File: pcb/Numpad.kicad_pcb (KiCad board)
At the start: 2 copper layers, 76.2 x 114.3 mm, 61 parts, among them P1 USB-MICRO-B, P2 HOLE, P3 HOLE, P4 HOLE, P5 HOLE, SW1 F13, SW10 8, SW11 9, SW12 PLUS, SW13 4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

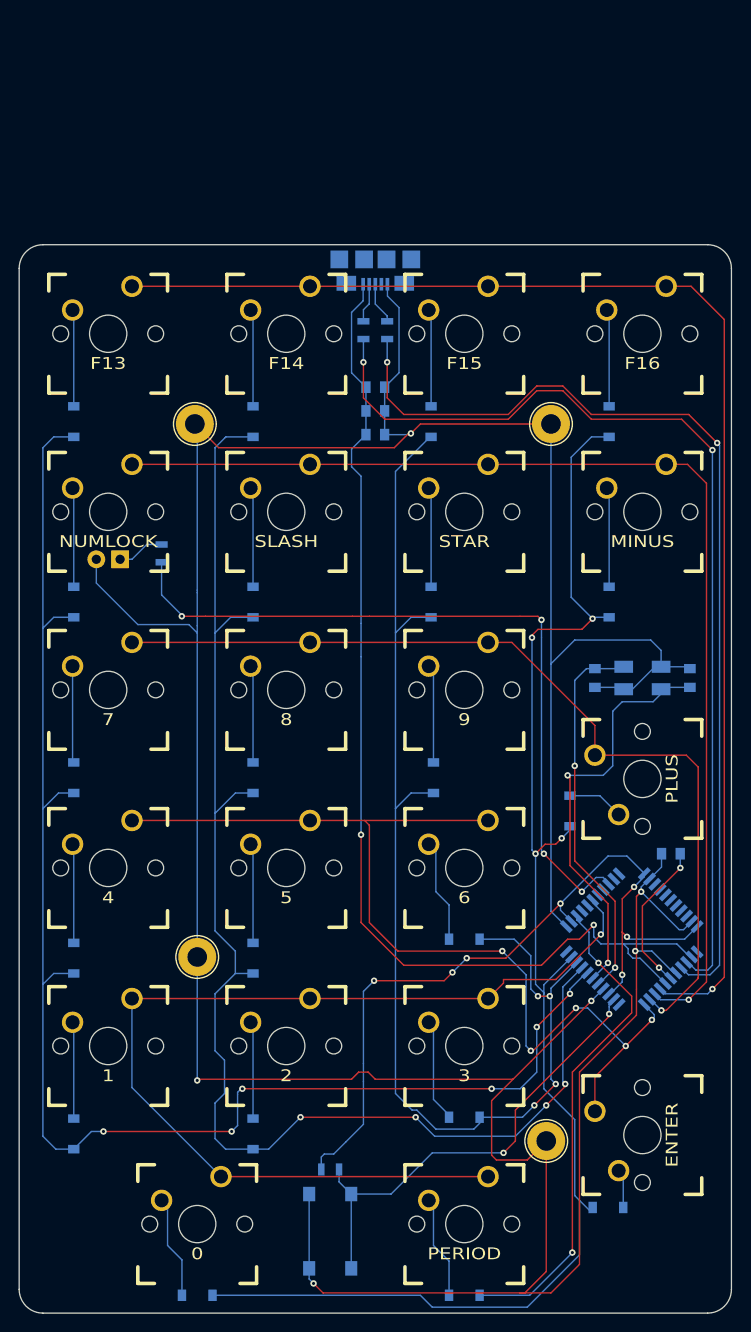
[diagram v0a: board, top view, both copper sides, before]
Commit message: Fix VCC/+5V problem. Shrink board by like 10 mils
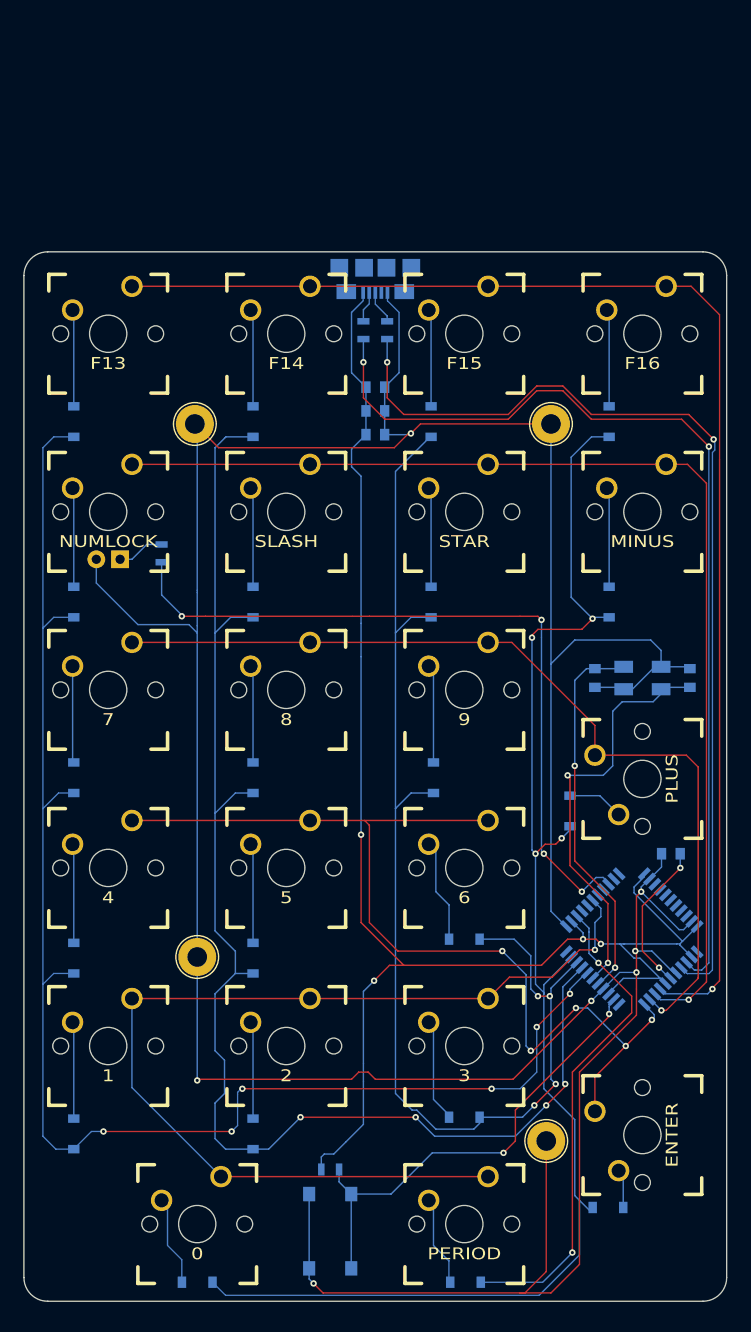
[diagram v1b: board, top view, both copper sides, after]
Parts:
- moved D21 1.40 mm to (113.8, 165.6)
- moved D20 1.40 mm to (85.1, 165.6)
- moved P1 0.89 mm to (104.1, 55.6)
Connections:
- R4 pad 2: VCC -> +5V
- U1 pad 14: VCC -> +5V
- U1 pad 24: VCC -> +5V
- U1 pad 34: VCC -> +5V
- U1 pad 44: VCC -> +5V
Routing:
- net VCC: track 84.3 -> 0.00 mm, vias 7 -> 0
- net +5V: track 118.3 -> 164.8 mm, vias 2 -> 4
- net GND: track 409.4 -> 396.9 mm, vias 6 -> 7
- net Net-(D20-Pad2): track 11.1 -> 9.66 mm
- net Net-(D21-Pad2): track 11.1 -> 9.74 mm
- net Net-(P1-Pad2): track 4.22 -> 3.33 mm
- net Net-(P1-Pad3): track 4.49 -> 3.60 mm
- net /COL4: track 52.9 -> 52.2 mm
- net Net-(R1-Pad1): track 106.9 -> 106.3 mm
- net Net-(R2-Pad1): track 106.9 -> 106.4 mm
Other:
- board size 76.2 x 114.3 mm -> 75.2 x 112.3 mm
- net class Default: clearance 0.1524 -> 0.127; trace_width 0.1524 -> 0.127
- rule trace_clearance: 0.1524 -> 0.127
- rule trace_min: 0.1524 -> 0.127

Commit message: Macrofab order
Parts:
- C2, C3: value 18p -> 8p
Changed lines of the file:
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@@
     (links 107)
     (no_connects 0)
-    (area 66.497999 55.321999 141.782001 167.690001)
+    (area 65.963799 54.123599 142.316201 168.986201)
     (thickness 1.6)
     (drawings 8)
@@
     (visible_elements 7FFFFFFF)
     (pcbplotparams
-      (layerselection 0x01000_00000000)
+      (layerselection 0x00030_00000000)
       (usegerberextensions false)
       (excludeedgelayer true)
@@
       (drillshape 0)
       (scaleselection 1)
-      (outputdirectory ../../../../../Desktop/))
+      (outputdirectory fab/))
   )
   (net 0 "")
@@
       (effects (font (size 0.5 0.5) (thickness 0.1)) (justify mirror))
     )
-    (fp_text value 18p (at -2.21 -0.01 180) (layer B.SilkS)
+    (fp_text value 8p (at -2.21 -0.01 180) (layer B.SilkS)
       (effects (font (size 0.5 0.5) (thickness 0.1)) (justify mirror))
     )
@@
       (effects (font (size 0.5 0.5) (thickness 0.1)) (justify mirror))
     )
-    (fp_text value 18p (at 2.21 -0.01 360) (layer B.SilkS)
+    (fp_text value 8p (at 2.21 -0.01 360) (layer B.SilkS)
       (effects (font (size 0.5 0.5) (thickness 0.1)) (justify mirror))
     )
@@
   (segment (start 135.61693 133.07693) (end 135.74393 133.07693) (width 0.1524) (layer B.Cu) (net 1))
   (segment (start 106.68 61.849) (end 105.44 60.609) (width 0.127) (layer B.Cu) (net 2))
-  (segment (start 105.44 60.609) (end 105.44 59.726) (width 0.127) (layer B.Cu) (net 2) (status 800000))
+  (segment (start 105.44 60.609) (end 105.44 59.726) (width 0.127) (layer B.Cu) (net 2))
   (segment (start 128.531441 134.208301) (end 130.278742 132.461) (width 0.127) (layer B.Cu) (net 2))
   (via (at 132.08 132.461) (size 0.6858) (drill 0.3302) (layers F.Cu B.Cu) (net 2))
@@
   (segment (start 127.635 99.965) (end 130.515 99.965) (width 0.1524) (layer B.Cu) (net 4))
   (segment (start 130.515 99.965) (end 130.715 99.765) (width 0.1524) (layer B.Cu) (net 4))
-  (segment (start 102.84 59.726) (end 102.84 60.609) (width 0.127) (layer B.Cu) (net 5) (status 400000))
+  (segment (start 102.84 59.726) (end 102.84 60.609) (width 0.127) (layer B.Cu) (net 5))
   (segment (start 102.84 60.609) (end 101.6 61.849) (width 0.1524) (layer B.Cu) (net 5))
   (segment (start 101.6 61.849) (end 101.6 68.31) (width 0.1524) (layer B.Cu) (net 5))
@@
   (segment (start 79.69 86.68) (end 81.28 86.68) (width 0.1524) (layer B.Cu) (net 32))
   (segment (start 78.105 88.265) (end 79.69 86.68) (width 0.1524) (layer B.Cu) (net 32))
-  (segment (start 103.49 59.726) (end 103.49 60.945) (width 0.127) (layer B.Cu) (net 33) (status 400000))
+  (segment (start 103.49 59.726) (end 103.49 60.945) (width 0.127) (layer B.Cu) (net 33))
   (segment (start 103.49 60.945) (end 102.87 61.565) (width 0.1524) (layer B.Cu) (net 33))
   (segment (start 102.87 61.565) (end 102.87 62.804) (width 0.1524) (layer B.Cu) (net 33))
-  (segment (start 104.14 59.726) (end 104.14 60.96) (width 0.127) (layer B.Cu) (net 34) (status 400000))
+  (segment (start 104.14 59.726) (end 104.14 60.96) (width 0.127) (layer B.Cu) (net 34))
   (segment (start 104.14 60.96) (end 105.41 62.23) (width 0.1524) (layer B.Cu) (net 34))
   (segment (start 105.41 62.23) (end 105.41 62.804) (width 0.1524) (layer B.Cu) (net 34))

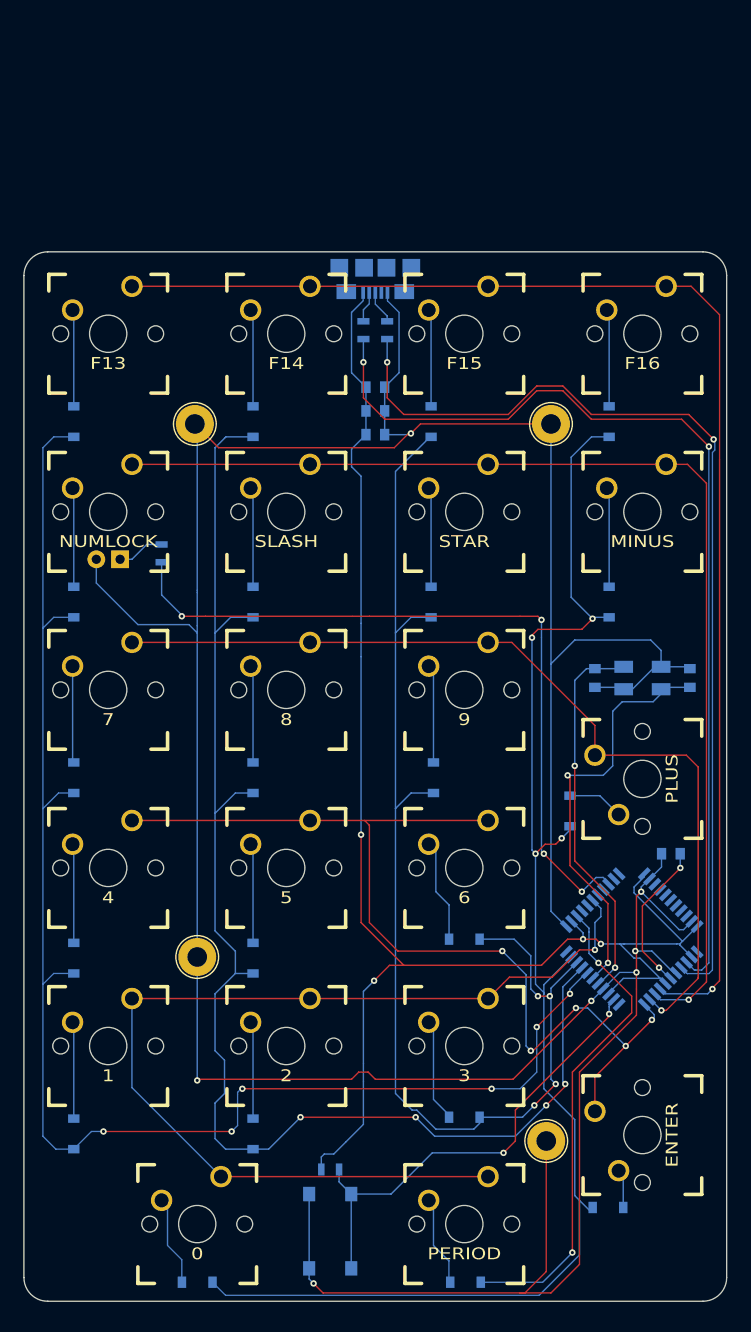
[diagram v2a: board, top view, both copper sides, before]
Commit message: Remove atmega32u4 and related components
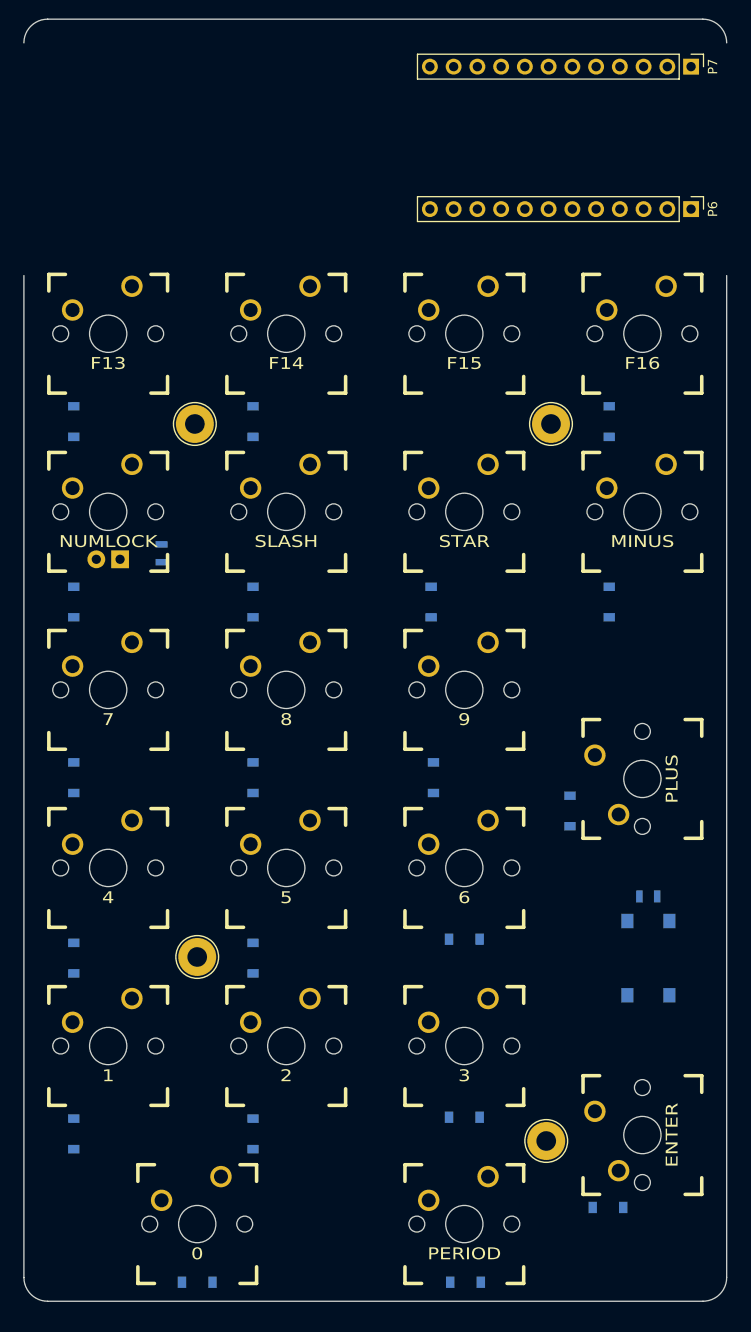
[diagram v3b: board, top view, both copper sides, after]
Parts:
- removed C1, C6: 1u, Keyboard:C_0805
- removed C2, C3: 8p, Keyboard:C_0805
- removed C4, C5: 0.1u, Keyboard:C_0805
- removed D3: D, Diodes_SMD:SOD-123
- removed P1: USB-MICRO-B, 10118192-0001LF:10118192-0001LF
- removed R1, R2: 22, Keyboard:R_0805
- removed U1: ATmega32U4-AU, ATMEGA32U4-AU:QFP80P1200X1200X120-44N
- removed X1: 16MHz, Crystals:Crystal_SMD_5032_4Pads
- added P6: CONN_01X12, Pin_Headers:Pin_Header_Straight_1x12_Pitch2.54mm, F.Cu at (137.9, 50.8)
- added P7: CONN_01X12, Pin_Headers:Pin_Header_Straight_1x12_Pitch2.54mm, F.Cu at (137.9, 35.6)
- moved R4 44.9 mm to (133.3, 124.3)
- moved SW22 44.9 mm to (133.3, 130.9)
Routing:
- net GND: track 396.9 -> 0.00 mm, vias 7 -> 0
- net +5V: track 164.8 -> 0.00 mm, vias 4 -> 0
- net /COL0: track 160.8 -> 0.00 mm, vias 6 -> 0
- net /COL3: track 154.1 -> 0.00 mm, vias 4 -> 0
- net /COL1: track 148.8 -> 0.00 mm, vias 4 -> 0
- net /ROW0: track 142.6 -> 0.00 mm, vias 1 -> 0
- net /COL2: track 128.8 -> 0.00 mm, vias 4 -> 0
- net /ROW1: track 122.2 -> 0.00 mm, vias 1 -> 0
- net /ROW4: track 109.2 -> 0.00 mm, vias 1 -> 0
- net Net-(R2-Pad1): track 106.4 -> 0.00 mm, vias 2 -> 0
- net Net-(R1-Pad1): track 106.3 -> 0.00 mm, vias 2 -> 0
- net /ROW3: track 104.9 -> 0.00 mm, vias 5 -> 0
- net /ROW2: track 97.9 -> 0.00 mm, vias 1 -> 0
- net /NUMLOCK_LED: track 80.1 -> 0.00 mm, vias 4 -> 0
- net /COL4: track 52.2 -> 0.00 mm, vias 2 -> 0
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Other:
- board size 75.2 x 112.3 mm -> 75.2 x 137.2 mm

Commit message: Complete routes and layout. Need to check Osh Park rules
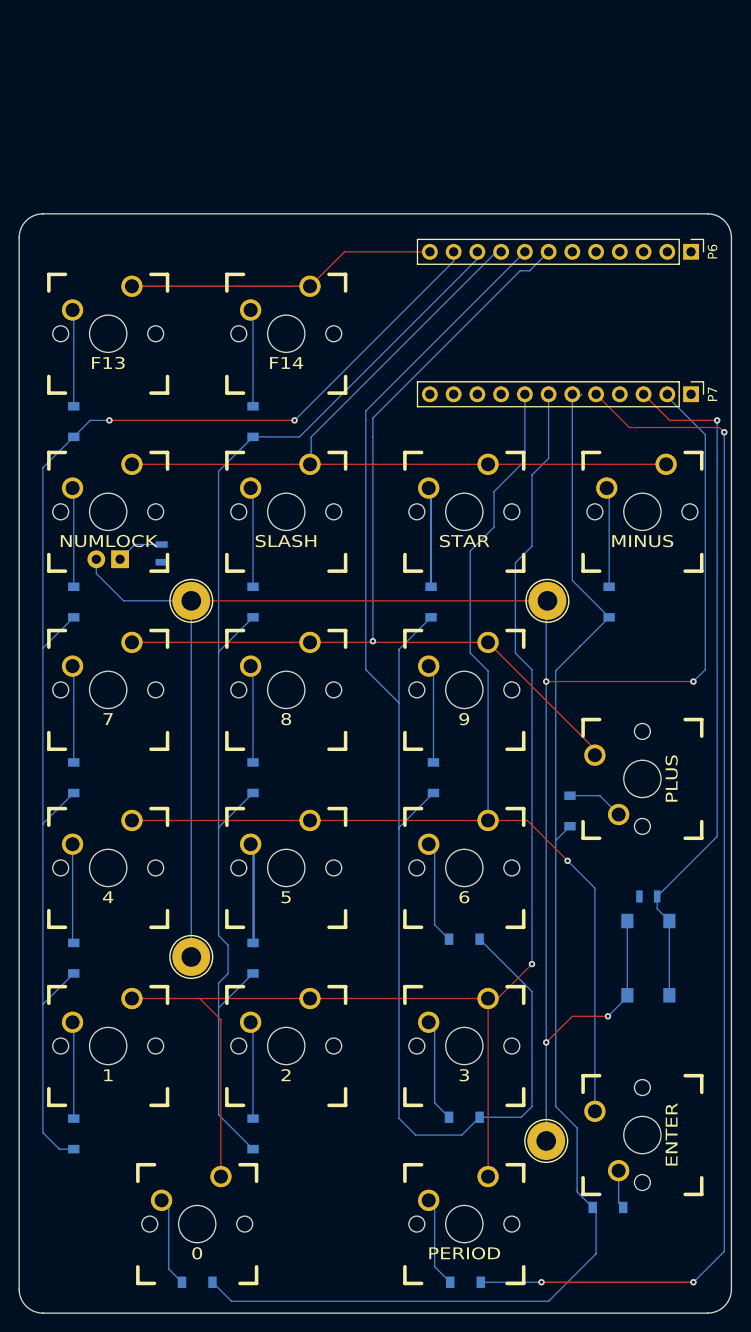
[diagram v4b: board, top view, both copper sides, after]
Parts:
- removed D4: D, Diodes_SMD:SOD-123
- removed SW3: F15, Tim's Cherry MX:CHERRY_PLATE_100H
- removed SW4: F16, Tim's Cherry MX:CHERRY_PLATE_100H
- moved P7 35.1 mm to (137.9, 70.6)
- moved P2 18.9 mm to (84.5, 92.7)
- moved P3 18.9 mm to (122.6, 92.7)
- moved P6 4.57 mm to (137.9, 55.4)
- moved P4 0.64 mm to (84.5, 130.8)
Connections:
- P6 pad 10: /ROW3 -> /COL1
- P6 pad 11: /ROW4 -> /COL0
- P6 pad 12: /COL0 -> /ROW0
- P6 pad 7: /ROW0 -> /ROW2
- P6 pad 8: /ROW1 -> /COL2
- P6 pad 9: /ROW2 -> /ROW1
- P7 pad 2: Net-(P7-Pad2) -> GND
- P7 pad 5: /COL1 -> /COL4
- P7 pad 6: /COL2 -> /COL3
- P7 pad 7: /COL3 -> /ROW4
- P7 pad 8: /COL4 -> /ROW3
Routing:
- net GND: track 0.00 -> 214.8 mm, vias 0 -> 4
- net /COL2: track 0.00 -> 153.6 mm
- net /ROW4: track 0.00 -> 146.5 mm, vias 0 -> 1
- net /COL3: track 0.00 -> 144.3 mm
- net /COL0: track 0.00 -> 143.6 mm, vias 0 -> 2
- net /COL4: track 0.00 -> 130.4 mm, vias 0 -> 3
- net /COL1: track 0.00 -> 128.8 mm
- net /ROW3: track 0.00 -> 125.2 mm, vias 0 -> 1
- net /ROW2: track 0.00 -> 105.1 mm, vias 0 -> 1
- net /ROW1: track 0.00 -> 88.7 mm
- net /ISP_RESET: track 0.00 -> 73.7 mm, vias 0 -> 1
- net /ROW0: track 0.00 -> 33.6 mm
- net Net-(D14-Pad2): track 0.00 -> 21.9 mm
- net Net-(D7-Pad2): track 0.00 -> 21.0 mm
- net Net-(D19-Pad2): track 0.00 -> 11.1 mm
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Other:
- board size 75.2 x 137.2 mm -> 76.2 x 117.6 mm

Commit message: fix track widths for Osh Park
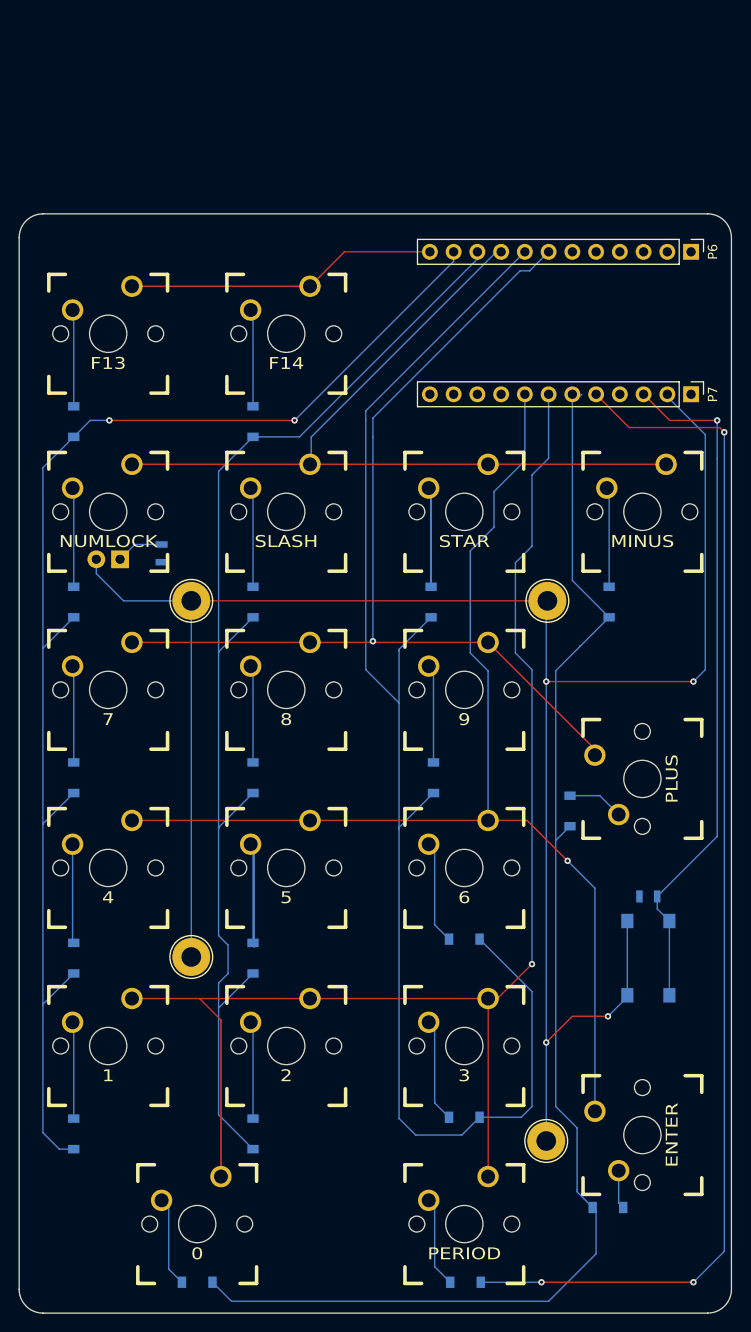
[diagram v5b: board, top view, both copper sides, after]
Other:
- net class Default: clearance 0.127 -> 0.1524; trace_width 0.127 -> 0.1524
- rule trace_clearance: 0.127 -> 0.1524
- rule trace_min: 0.127 -> 0.1524
